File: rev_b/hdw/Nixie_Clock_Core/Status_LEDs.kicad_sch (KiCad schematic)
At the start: 20 parts, among them U1701 74LVC1G06, U1702 74LVC1G06, U1703 74LVC1G06, U1704 74LVC1G06

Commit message: lots of rev B control board schematic progress
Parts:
- renumbered U1703 to U?, U1704 to U?, U1702 to U?, U1701 to U?

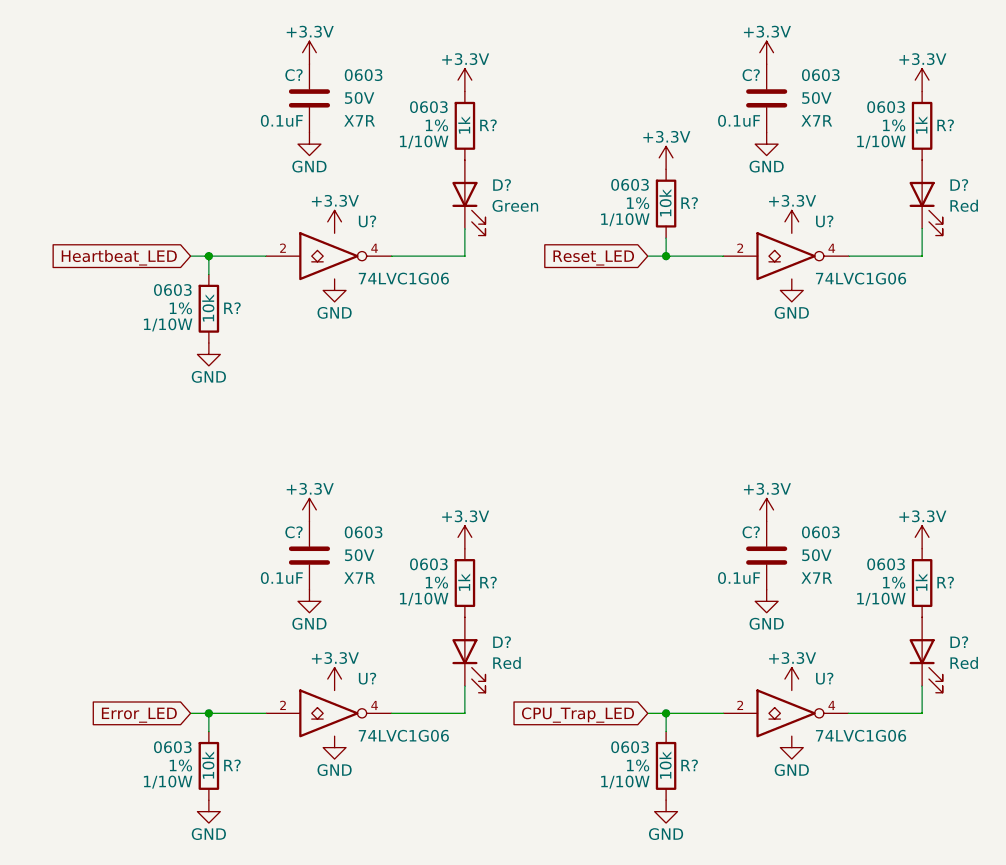
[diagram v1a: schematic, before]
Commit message: more schematic progress, assigning signals to MCU"
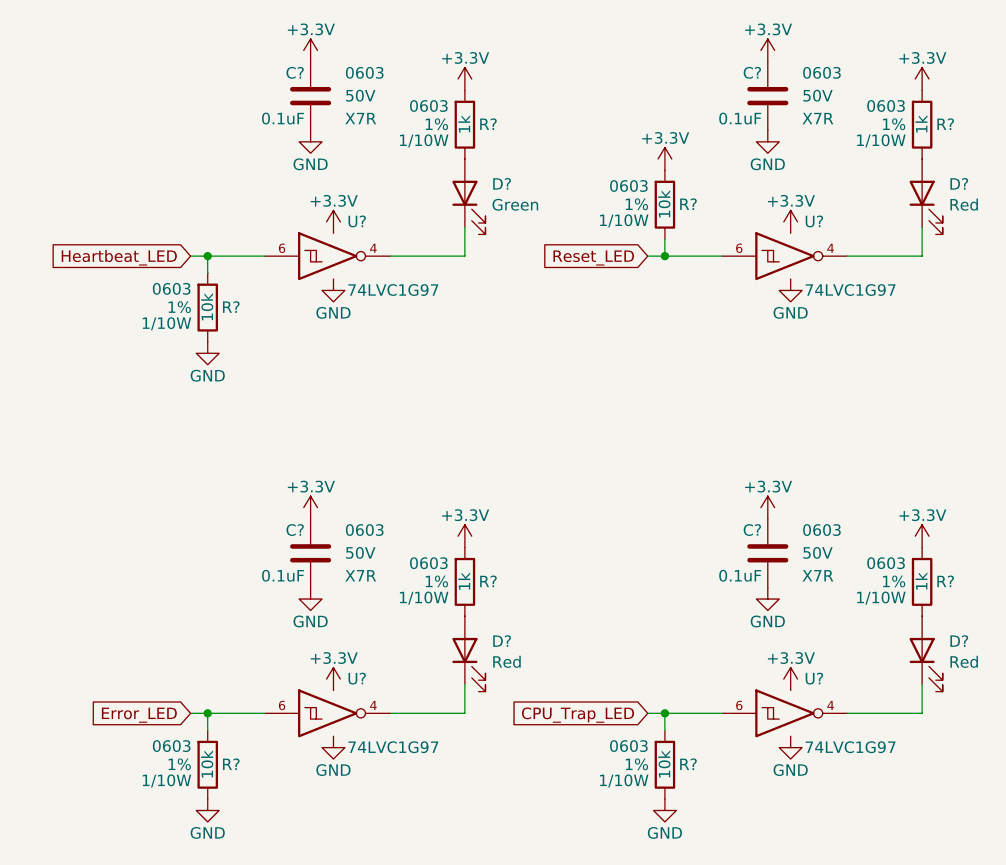
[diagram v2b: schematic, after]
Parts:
- removed U? (x4): 74LVC1G06, TO_SOT_Packages_SMD:SOT-353_SC-70-5, symbol Custom_Library:74LVC1G06_Power
- added U? (x4): 74LVC1G97, Package_TO_SOT_SMD:SOT-363_SC-70-6, symbol Custom Library:74LVC1G97_Power_NOT
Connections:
- net +3.3V: now also U?.1 (VCC), U?.1 (VCC), U?.1 (VCC), U?.1 (VCC), U?.5 (VCC), U?.5 (VCC), U?.5 (VCC), U?.5 (VCC)
- net CPU_Trap_LED: now also U?.6
- net Error_LED: now also U?.6
- net GND: now also U?.2 (GND), U?.2 (GND), U?.2 (GND), U?.2 (GND), U?.3 (GND), U?.3 (GND), U?.3 (GND), U?.3 (GND)
- net Heartbeat_LED: now also U?.6
- net Reset_LED: now also U?.6
- net at D?.1 (K): now also U?.4 (x4)

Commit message: updated footprints, ran some DRC
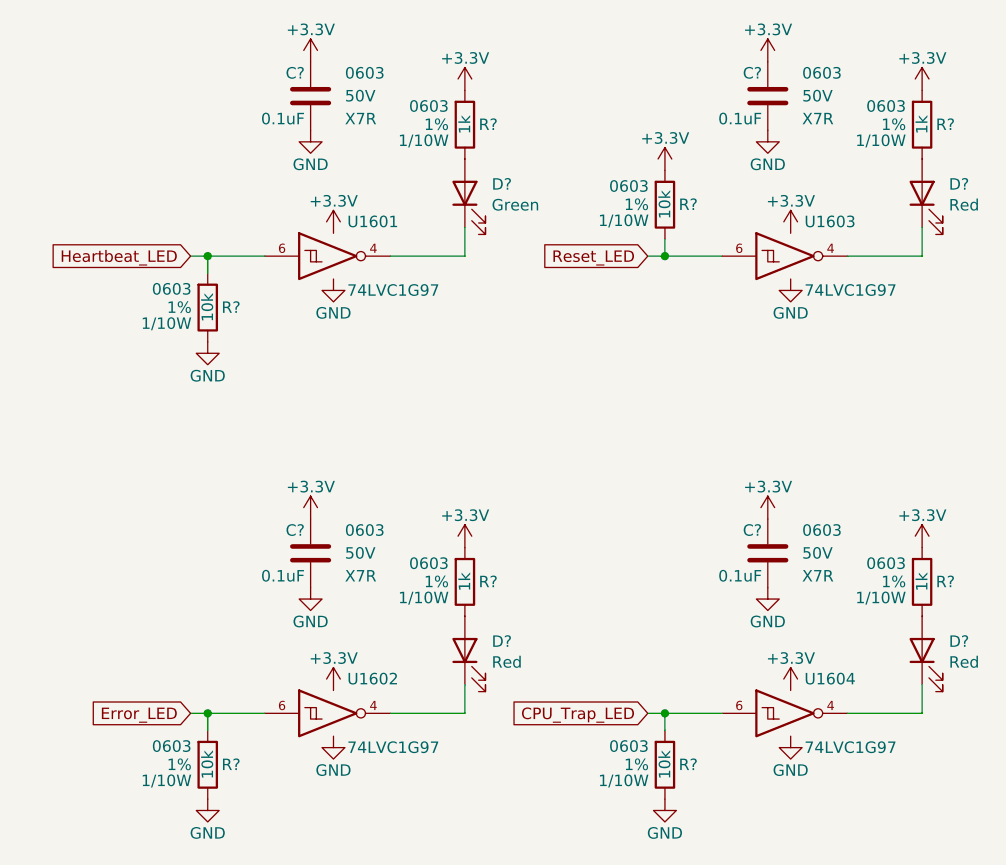
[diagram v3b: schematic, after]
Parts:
- C? (x4): Digi-Key PN 399-7845-1-ND -> (none)
- R? (x4): Digi-Key PN 311-1.00KHRCT-ND -> (none)
- R? (x4): Digi-Key PN YAG2321CT-ND -> (none)
- gave numbers to parts that had none: 4

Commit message: hid all passive refdes on core PCB
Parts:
- C? (x4): Digi-Key PN (none) -> 1276-1935-1-ND
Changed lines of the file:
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@@
       (effects (font (size 1.27 1.27)) hide)
     )
-    (property "Digi-Key PN" "" (at 86.36 93.98 0)
+    (property "Digi-Key PN" "1276-1935-1-ND" (at 86.36 93.98 0)
       (effects (font (size 1.524 1.524)) hide)
     )
@@
       (effects (font (size 1.27 1.27)) hide)
     )
-    (property "Digi-Key PN" "" (at 137.16 93.98 0)
+    (property "Digi-Key PN" "1276-1935-1-ND" (at 137.16 93.98 0)
       (effects (font (size 1.524 1.524)) hide)
     )
@@
       (effects (font (size 1.27 1.27)) hide)
     )
-    (property "Digi-Key PN" "" (at 86.36 43.18 0)
+    (property "Digi-Key PN" "1276-1935-1-ND" (at 86.36 43.18 0)
       (effects (font (size 1.524 1.524)) hide)
     )
@@
       (effects (font (size 1.27 1.27)) hide)
     )
-    (property "Digi-Key PN" "" (at 137.16 43.18 0)
+    (property "Digi-Key PN" "1276-1935-1-ND" (at 137.16 43.18 0)
       (effects (font (size 1.524 1.524)) hide)
     )

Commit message: added BOM
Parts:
- R? (x4): Digi-Key PN (none) -> 541-1.00KHCT-ND
- R? (x4): Digi-Key PN (none) -> 541-10.0KHCT-ND
- U1601, U1602, U1603, U1604: Digi-Key PN (none) -> 296-15582-1-ND
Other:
- title: (none) -> Nixie Clock Redux Core Board
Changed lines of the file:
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@@
   (paper "A")
   (title_block
-    (date "2023-05-12")
-    (rev "PRELIM")
+    (title "Nixie Clock Redux Core Board")
+    (date "2023-07-30")
+    (rev "B")
     (company "Drew Maatman")
   )
@@
     (stroke (width 0) (type default))
   )
-  (global_label "Reset_LED" (shape input) (at 134.62 73.66 180)
+  (global_label "Reset_LED" (shape input) (at 134.62 73.66 180) (fields_autoplaced)
     (effects (font (size 1.27 1.27)) (justify right))
-    (property "Intersheetrefs" "${INTERSHEET_REFS}" (at 134.62 73.66 0)
-      (effects (font (size 1.27 1.27)) hide)
-    )
-  )
-  (global_label "Heartbeat_LED" (shape input) (at 83.82 73.66 180)
+    (property "Intersheetrefs" "${INTERSHEET_REFS}" (at 122.0985 73.66 0)
+      (effects (font (size 1.27 1.27)) (justify right))
+    )
+  )
+  (global_label "Heartbeat_LED" (shape input) (at 83.82 73.66 180) (fields_autoplaced)
     (effects (font (size 1.27 1.27)) (justify right))
-    (property "Intersheetrefs" "${INTERSHEET_REFS}" (at 83.82 73.66 0)
-      (effects (font (size 1.27 1.27)) hide)
-    )
-  )
-  (global_label "Error_LED" (shape input) (at 83.82 124.46 180)
+    (property "Intersheetrefs" "${INTERSHEET_REFS}" (at 67.3072 73.66 0)
+      (effects (font (size 1.27 1.27)) (justify right))
+    )
+  )
+  (global_label "Error_LED" (shape input) (at 83.82 124.46 180) (fields_autoplaced)
     (effects (font (size 1.27 1.27)) (justify right))
-    (property "Intersheetrefs" "${INTERSHEET_REFS}" (at 83.82 124.46 0)
-      (effects (font (size 1.27 1.27)) hide)
-    )
-  )
-  (global_label "CPU_Trap_LED" (shape input) (at 134.62 124.46 180)
+    (property "Intersheetrefs" "${INTERSHEET_REFS}" (at 71.8429 124.46 0)
+      (effects (font (size 1.27 1.27)) (justify right))
+    )
+  )
+  (global_label "CPU_Trap_LED" (shape input) (at 134.62 124.46 180) (fields_autoplaced)
     (effects (font (size 1.27 1.27)) (justify right))
-    (property "Intersheetrefs" "${INTERSHEET_REFS}" (at 134.62 124.46 0)
-      (effects (font (size 1.27 1.27)) hide)
+    (property "Intersheetrefs" "${INTERSHEET_REFS}" (at 118.4096 124.46 0)
+      (effects (font (size 1.27 1.27)) (justify right))
     )
   )
@@
       (effects (font (size 1.27 1.27)) (justify left))
     )
-    (property "Digi-Key PN" "" (at 157.48 48.895 0)
+    (property "Digi-Key PN" "541-1.00KHCT-ND" (at 157.48 48.895 0)
       (effects (font (size 1.524 1.524)) hide)
     )
@@
     )
     (property "Datasheet" "http://www.ti.com/lit/ds/symlink/sn74lvc1g97.pdf" (at 100.965 73.66 0)
+      (effects (font (size 1.27 1.27)) hide)
+    )
+    (property "Digi-Key PN" "296-15582-1-ND" (at 99.695 73.66 0)
       (effects (font (size 1.27 1.27)) hide)
     )
@@
       (effects (font (size 1.27 1.27)) (justify left))
     )
-    (property "Digi-Key PN" "" (at 85.725 79.375 0)
+    (property "Digi-Key PN" "541-10.0KHCT-ND" (at 85.725 79.375 0)
       (effects (font (size 1.27 1.27)) hide)
     )
@@
     )
     (property "Datasheet" "http://www.ti.com/lit/ds/symlink/sn74lvc1g97.pdf" (at 151.765 124.46 0)
+      (effects (font (size 1.27 1.27)) hide)
+    )
+    (property "Digi-Key PN" "296-15582-1-ND" (at 150.495 124.46 0)
       (effects (font (size 1.27 1.27)) hide)
     )
@@
       (effects (font (size 1.27 1.27)) (justify left))
     )
-    (property "Digi-Key PN" "" (at 136.525 130.175 0)
+    (property "Digi-Key PN" "541-10.0KHCT-ND" (at 136.525 130.175 0)
       (effects (font (size 1.27 1.27)) hide)
     )
@@
       (effects (font (size 1.27 1.27)) (justify left))
     )
-    (property "Digi-Key PN" "" (at 157.48 99.695 0)
+    (property "Digi-Key PN" "541-1.00KHCT-ND" (at 157.48 99.695 0)
       (effects (font (size 1.524 1.524)) hide)
     )
@@
     )
     (property "Datasheet" "http://www.ti.com/lit/ds/symlink/sn74lvc1g97.pdf" (at 151.765 73.66 0)
+      (effects (font (size 1.27 1.27)) hide)
+    )
+    (property "Digi-Key PN" "296-15582-1-ND" (at 150.495 73.66 0)
       (effects (font (size 1.27 1.27)) hide)
     )
@@
       (effects (font (size 1.27 1.27)) (justify left))
     )
-    (property "Digi-Key PN" "" (at 106.68 48.895 0)
+    (property "Digi-Key PN" "541-1.00KHCT-ND" (at 106.68 48.895 0)
       (effects (font (size 1.524 1.524)) hide)
     )
@@
       (effects (font (size 1.27 1.27)) (justify left))
     )
-    (property "Digi-Key PN" "" (at 136.525 67.945 0)
+    (property "Digi-Key PN" "541-10.0KHCT-ND" (at 136.525 67.945 0)
       (effects (font (size 1.27 1.27)) hide)
     )
@@
       (effects (font (size 1.27 1.27)) (justify left))
     )
-    (property "Digi-Key PN" "" (at 85.725 130.175 0)
+    (property "Digi-Key PN" "541-10.0KHCT-ND" (at 85.725 130.175 0)
       (effects (font (size 1.27 1.27)) hide)
     )
@@
       (effects (font (size 1.27 1.27)) (justify left))
     )
-    (property "Digi-Key PN" "" (at 106.68 99.695 0)
+    (property "Digi-Key PN" "541-1.00KHCT-ND" (at 106.68 99.695 0)
       (effects (font (size 1.524 1.524)) hide)
     )
@@
       (effects (font (size 1.27 1.27)) hide)
     )
+    (property "Digi-Key PN" "296-15582-1-ND" (at 99.695 124.46 0)
+      (effects (font (size 1.27 1.27)) hide)
+    )
